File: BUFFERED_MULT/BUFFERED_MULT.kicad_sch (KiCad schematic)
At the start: 13 parts, among them J1 AudioJack2, J2 AudioJack2, J3 AudioJack2, J4 AudioJack2, J5 AudioJack2, J6 Conn_02x05_Odd_Even, U1 2144_LPF

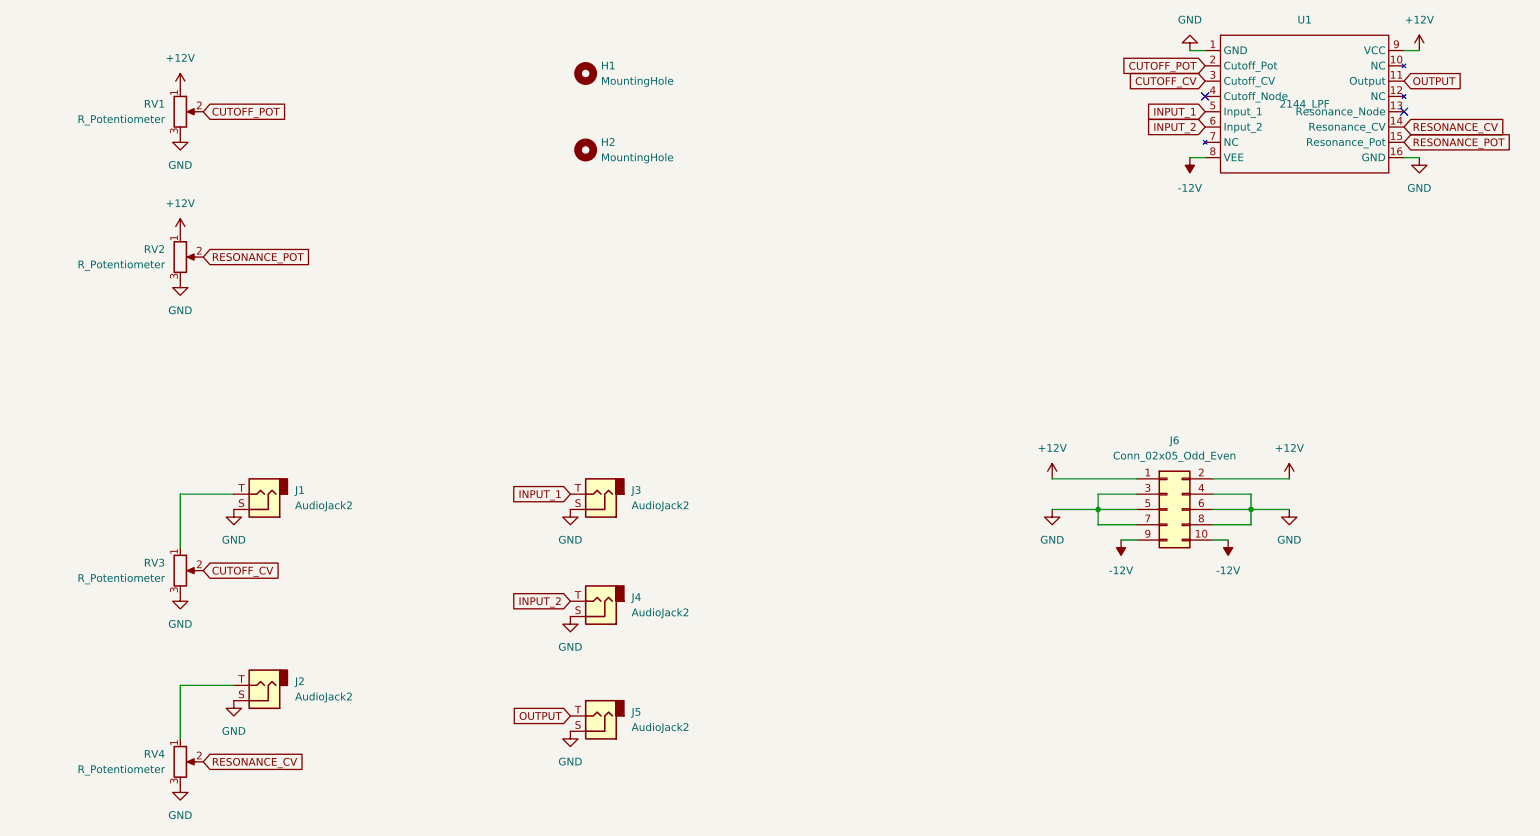
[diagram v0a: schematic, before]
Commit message: updating buffered mult schematic
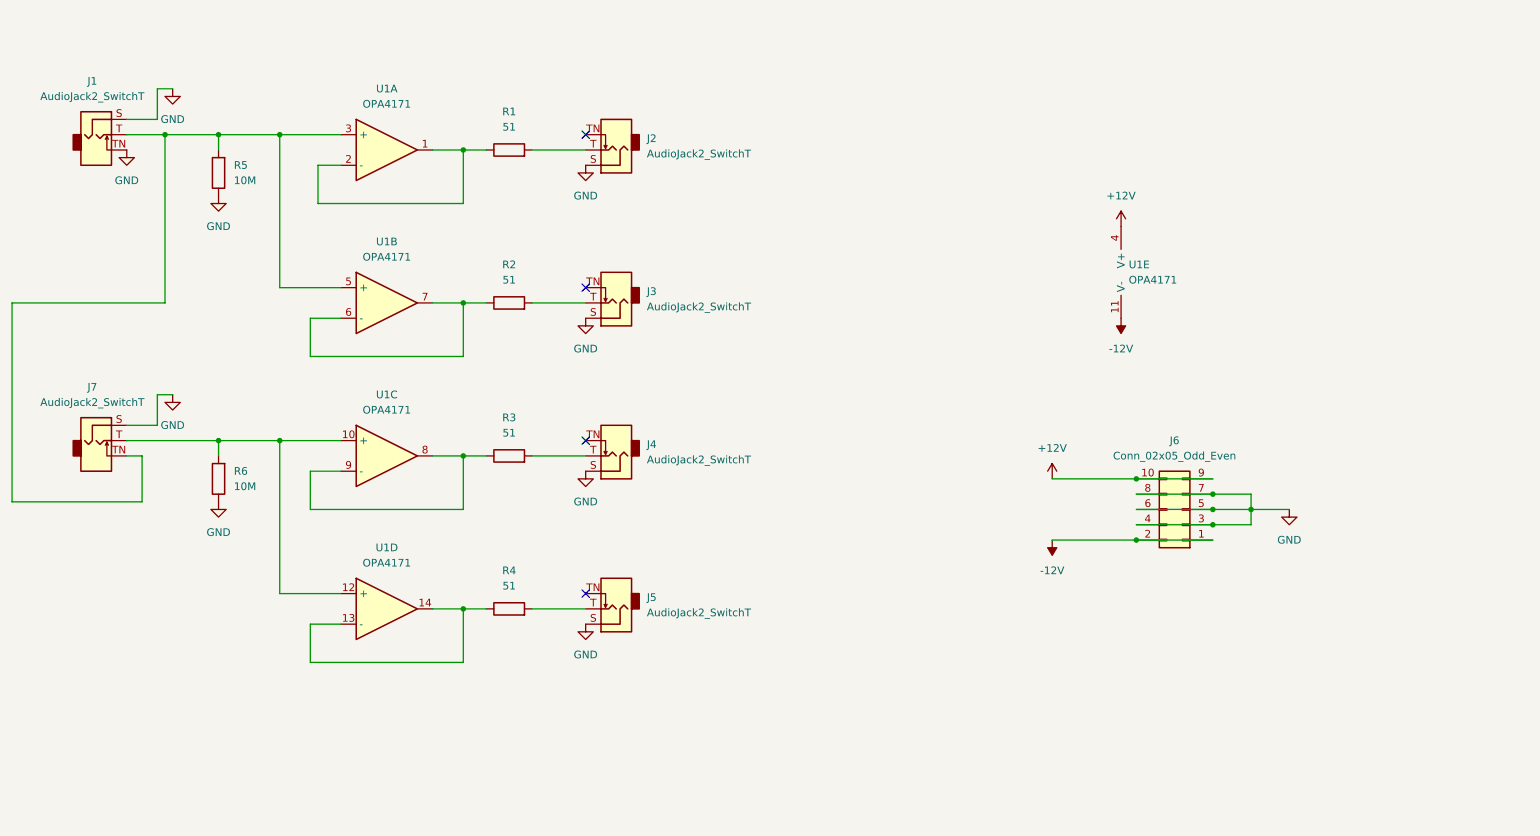
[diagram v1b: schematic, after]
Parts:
- removed H1, H2: MountingHole, MountingHole:MountingHole_3.2mm_M3, symbol Mechanical:MountingHole
- removed J1, J2, J3, J4, J5: AudioJack2, AudioJacks:Jack_3.5mm_QingPu_WQP-PJ398SM_Vertical, symbol Connector_Audio:AudioJack2
- removed RV1, RV2, RV3, RV4: R_Potentiometer, Potentiometer_THT:Potentiometer_Bourns_PTA4543_Single_Slide, symbol Device:R_Potentiometer
- removed U1: 2144_LPF, Dans_Eurorack:Electrosmith_2144_LPF, symbol Dans_Eurorack_Library:Electrosmith_2144_LPF
- added J1, J2, J3, J4, J5, J7: AudioJack2_SwitchT, AudioJacks:Jack_3.5mm_QingPu_WQP-PJ398SM_Vertical, symbol Connector_Audio:AudioJack2_SwitchT
- added R1, R2, R3, R4: 51, Resistor_SMD:R_0201_0603Metric, symbol Device:R
- added R5, R6: 10M, Resistor_SMD:R_0201_0603Metric, symbol Device:R
- added U1: OPA4171, Package_SO:TSSOP-14_4.4x5mm_P0.65mm, symbol Dans_Eurorack_Library:OPA4171
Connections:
- net +12V: now also J6.10 (Pin_10), J6.9 (Pin_9), U1.4 (V+); no longer J6.1 (Pin_1), J6.2 (Pin_2)
- net -12V: now also J6.1 (Pin_1), J6.2 (Pin_2), U1.11 (V-); no longer J6.10 (Pin_10), J6.9 (Pin_9)
- net GND: now also J1.S, J1.TN, J2.S, J3.S, J4.S, J5.S, J7.S, R5.1, R6.1
- new net: R4.1, U1.13 (-), U1.14
- new net: J5.T, R4.2
- new net: J7.T, R6.2, U1.10 (+), U1.12 (+)
- new net: J1.T, J7.TN, R5.2, U1.3 (+), U1.5 (+)
- new net: R3.1, U1.8, U1.9 (-)
- new net: J4.T, R3.2
- new net: R1.1, U1.1, U1.2 (-)
- new net: J2.T, R1.2
- new net: J3.T, R2.2
- new net: R2.1, U1.6 (-), U1.7
- no-connect marks 2 -> 4
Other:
- moved on the sheet: J6
